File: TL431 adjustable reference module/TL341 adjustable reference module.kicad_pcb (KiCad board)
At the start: 2 copper layers, 11.2 x 20.3 mm, 7 parts, among them J1 Conn_01x04_Male, U1 TL431LP

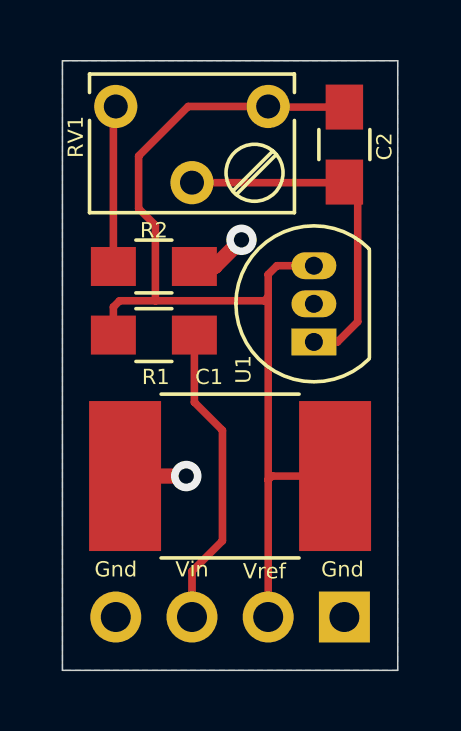
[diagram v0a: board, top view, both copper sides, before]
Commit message: Silk screen edits
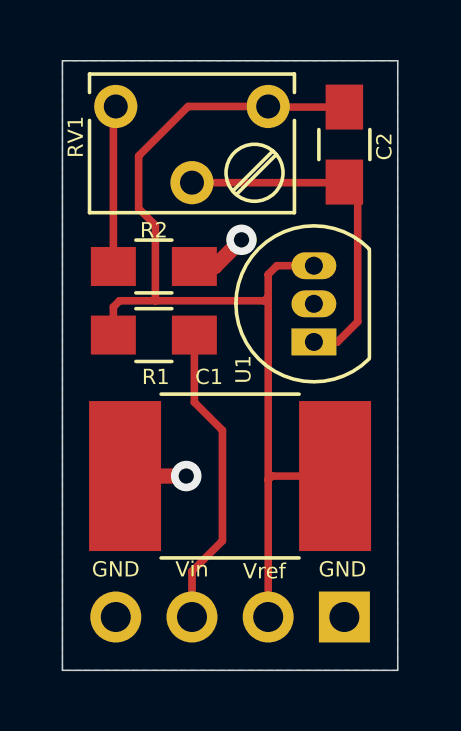
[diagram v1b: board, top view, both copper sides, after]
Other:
- board text added: "GND"
- board text added: "TL431 Voltage Reference Rev A 2021 Bobrowicz, P."
- board text removed: "Gnd"
- board text removed: "TL431 Voltage Reference Rev A Bobrowicz, P."
